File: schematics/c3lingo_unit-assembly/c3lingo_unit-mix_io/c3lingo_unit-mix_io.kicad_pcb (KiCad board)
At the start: 2 copper layers, 80 x 50 mm, 47 parts, among them J201 Stage Line-In, J202 Mix Line-Out, J203 PowerSupply, J204 Ch1, J205 Ch2, J206 Ch3, SW201 GND Lift, U201 LM833-N, U202 DRV135UA, U203 LM833-N

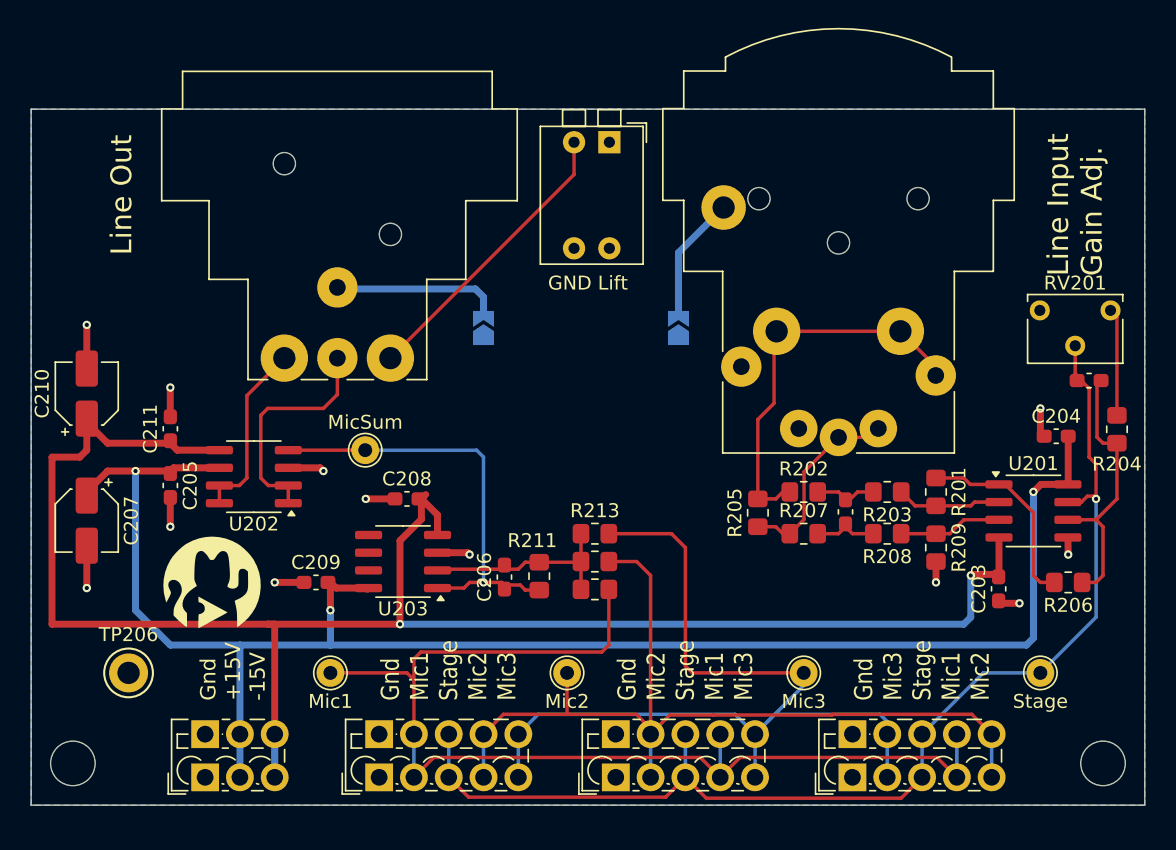
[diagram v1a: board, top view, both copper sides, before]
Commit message: Line I/O: Optimize Schematic and update PCB
Share one LM833 instead of only using one half for summing and line input each.
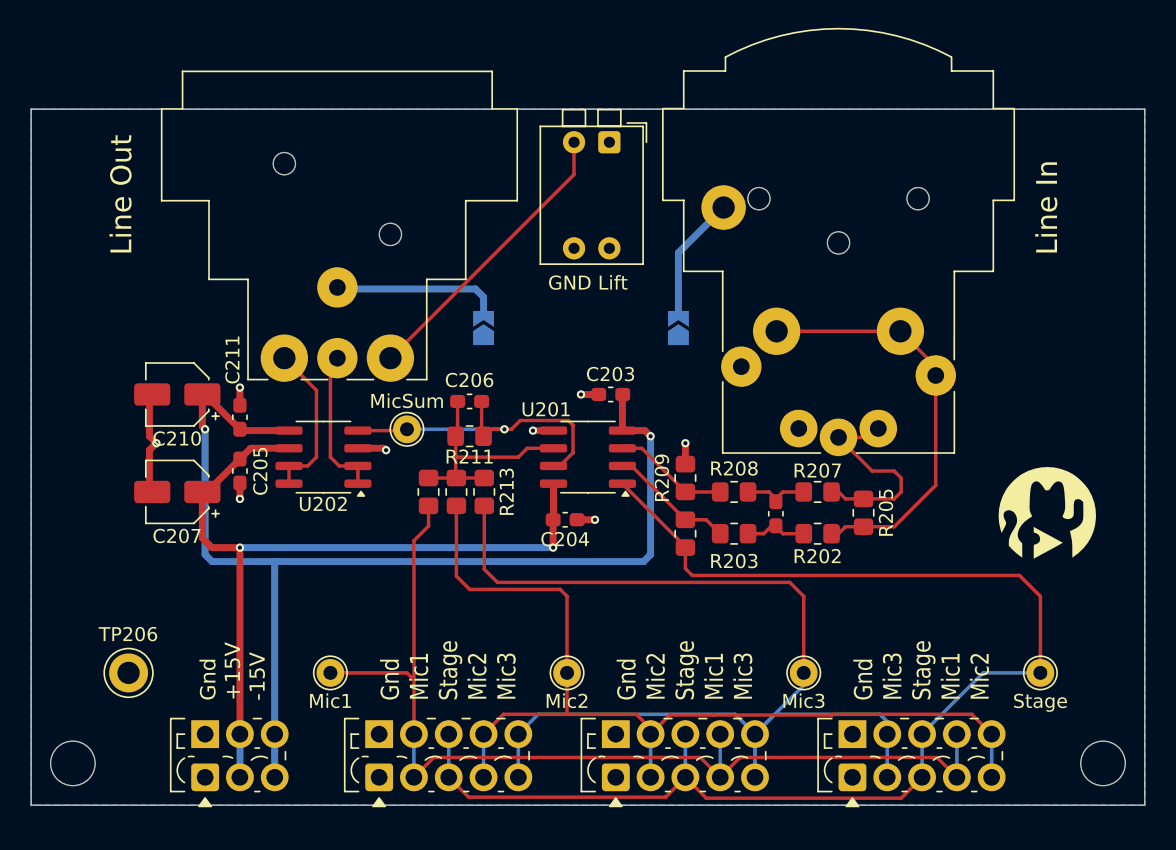
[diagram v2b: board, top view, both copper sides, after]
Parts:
- removed C201: 47pF, Capacitor_SMD:C_0603_1608Metric_Pad1.08x0.95mm_HandSolder
- removed C208, C209: 100nF, Capacitor_SMD:C_0603_1608Metric_Pad1.08x0.95mm_HandSolder
- removed R204: 22K, Resistor_SMD:R_0805_2012Metric_Pad1.20x1.40mm_HandSolder
- removed R206: 47K, Resistor_SMD:R_0805_2012Metric_Pad1.20x1.40mm_HandSolder
- removed RV201: 100K, Potentiometer_THT:Potentiometer_Vishay_T73XX_Horizontal
- removed U203: LM833-N, Package_SO:SOIC-8_3.9x4.9mm_P1.27mm
- R211: value 22K -> 10K
- moved G*** 60.2 mm to (133.0, 79.0)
- moved C204 35.8 mm to (98.4, 79.5), turned to 180 degrees
- moved U201 32.2 mm to (100.0, 75.0), turned to 180 degrees
- moved C203 31.2 mm to (101.6, 70.5), turned to 0 degrees
- moved R209 18.7 mm to (107.0, 76.5), turned to 90 degrees
- moved R201 18.2 mm to (107.0, 80.5), turned to 90 degrees
- moved R210 13.8 mm to (88.5, 77.5), turned to -90 degrees
- moved C206 12.9 mm to (91.5, 71.0), turned to 180 degrees
- moved R203 11.4 mm to (110.5, 80.5), turned to 0 degrees
- moved R208 11.4 mm to (110.5, 77.5), turned to 0 degrees
- moved R211 11.2 mm to (91.5, 73.5), turned to 180 degrees
- moved R212 11.1 mm to (90.5, 77.5), turned to -90 degrees
- moved R213 8.50 mm to (92.5, 77.5), turned to -90 degrees
- moved R205 7.59 mm to (119.8, 79.0), turned to -90 degrees
- moved C207 6.82 mm to (70.5, 77.5), turned to 180 degrees
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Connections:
- C206 pad 2: Net-(U203A--) -> Net-(U201B--)
- R201 pad 1: Net-(R201-Pad1) -> /Stage
- R210 pad 1: Net-(U203A--) -> Net-(U201B--)
- R211 pad 2: Net-(U203A--) -> Net-(U201B--)
- R212 pad 1: Net-(U203A--) -> Net-(U201B--)
- R213 pad 1: Net-(U203A--) -> Net-(U201B--)
- U201 pad 1: Net-(R201-Pad1) -> /Stage
- U201 pad 7: /Stage -> Net-(U202-VIN)
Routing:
- net +15V: track 119.2 -> 57.7 mm, vias 3 -> 2
- net -15V: track 125.6 -> 80.2 mm
- net Net-(U203A--): track 15.5 -> 0.00 mm
- net Net-(R201-Pad1): track 14.3 -> 0.00 mm
- net /Stage: track 84.1 -> 95.8 mm, vias 1 -> 0
- net /Mic_Ch3: track 67.7 -> 78.3 mm
- net Net-(R204-Pad1): track 7.73 -> 0.00 mm
- net Net-(U202-VIN): track 31.1 -> 23.9 mm
- net /Mic_Ch1: track 81.1 -> 74.2 mm
- net GND: track 24.6 -> 17.7 mm, vias 12 -> 8
- net Net-(U202-SENSE-): track 16.7 -> 10.8 mm
- net /Mic_Ch2: track 65.8 -> 70.1 mm
- net Net-(U201B--): track 20.7 -> 16.9 mm
- net Net-(J201-Pad2): track 28.2 -> 30.2 mm
- net Net-(U202-SENSE+): track 13.2 -> 11.6 mm
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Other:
- board text added: "Line In"
- board text added: "c3lingo Interpreter Unit Mix I/O v0.4.0-dev 2025-08-25"
- board text removed: "Line Input Gain Adj."
- board text removed: "c3lingo Interpreter Unit Mix I/O v0.3.3 2024-09-08"

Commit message: Change inter-PCB connections to IDC connectors
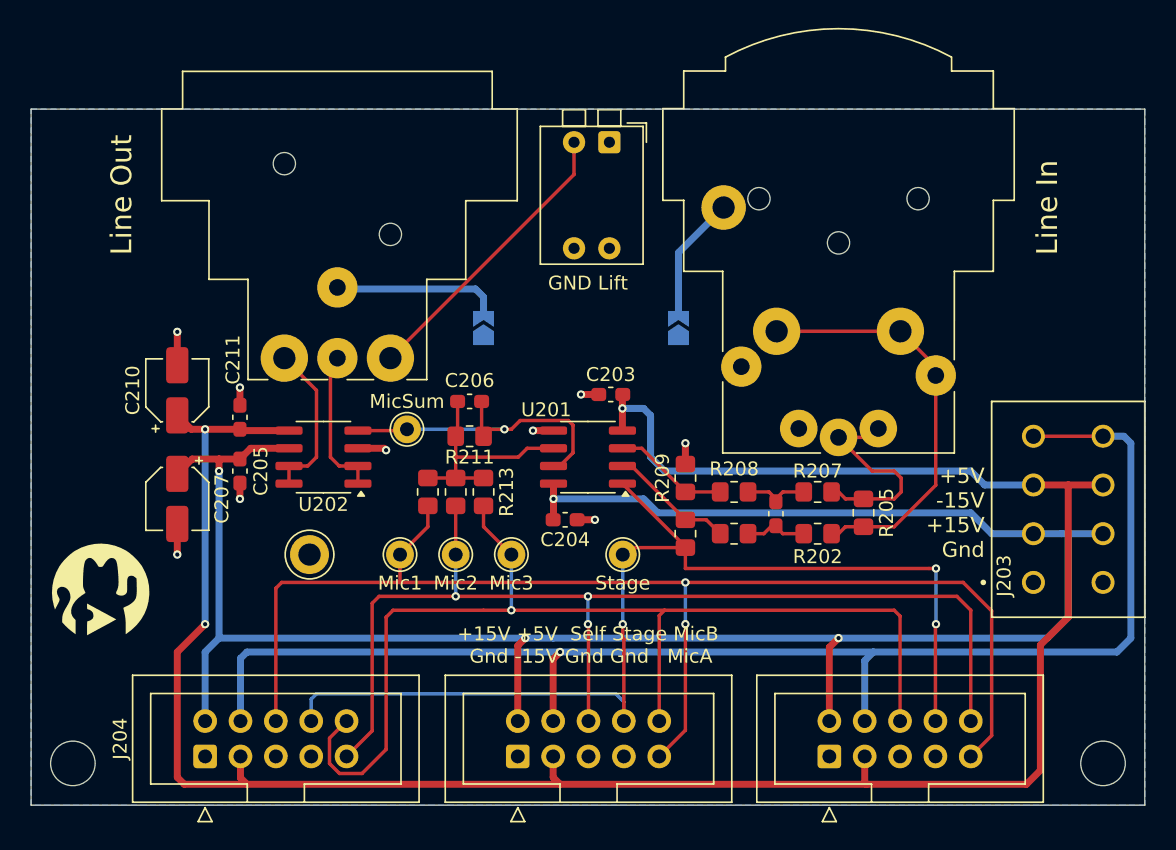
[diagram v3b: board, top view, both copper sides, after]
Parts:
- J203: footprint TerminalBlock_Phoenix:TerminalBlock_Phoenix_PTSM-0,5-3-2.5-V-THR_1x03_P2.50mm_Vertical -> c3lingo_unit-footprints:TerminalBlock_Phoenix_SPTAF-1-4-3.5_1x04_P3.5mm
- J204, J205, J206: footprint TerminalBlock_Phoenix:TerminalBlock_Phoenix_PTSM-0,5-5-2.5-V-THR_1x05_P2.50mm_Vertical -> Connector_IDC:IDC-Header_2x05_P2.54mm_Vertical
- moved J203 68.5 mm to (140.0, 86.5), turned to 90 degrees
- moved G*** 68.2 mm to (65.0, 84.5)
- moved TP201 31.2 mm to (102.5, 82.0)
- moved TP205 22.7 mm to (94.5, 82.0)
- moved TP206 15.5 mm to (80.0, 82.0)
- moved J204 12.6 mm to (72.5, 96.5), turned to 90 degrees
- moved TP203 11.7 mm to (90.5, 82.0)
- moved TP202 9.86 mm to (86.5, 82.0)
- moved J205 7.20 mm to (95.0, 96.5), turned to 90 degrees
- moved J206 2.24 mm to (117.3, 96.5), turned to 90 degrees
- moved C207 0.50 mm to (70.5, 78.0), turned to -90 degrees
- moved C210 0.30 mm to (70.5, 70.2), turned to 90 degrees
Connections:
- J204 pad 2: /Mic_Ch1 -> +15V
- J204 pad 3: /Stage -> -15V
- J204 pad 4: /Mic_Ch2 -> +5V
- J204 pad 5: /Mic_Ch3 -> GND
- J205 pad 2: /Mic_Ch2 -> +15V
- J205 pad 3: /Stage -> -15V
- J205 pad 4: /Mic_Ch1 -> +5V
- J205 pad 5: /Mic_Ch3 -> GND
- J206 pad 2: /Mic_Ch3 -> +15V
- J206 pad 3: /Stage -> -15V
- J206 pad 4: /Mic_Ch1 -> +5V
- J206 pad 5: /Mic_Ch2 -> GND
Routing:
- net +5V: track 0.00 -> 100.7 mm, vias 0 -> 1
- net +15V: track 57.7 -> 151.2 mm, vias 2 -> 4
- net -15V: track 80.2 -> 165.9 mm, vias 2 -> 3
- net /Mic_Ch1: track 74.2 -> 92.7 mm, vias 0 -> 2
- net /Stage: track 95.8 -> 79.3 mm, vias 0 -> 3
- net /Mic_Ch2: track 70.1 -> 78.8 mm, vias 0 -> 3
- net GND: track 17.7 -> 14.6 mm, vias 8 -> 9
- net /Mic_Ch3: track 78.3 -> 79.4 mm, vias 0 -> 1
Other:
- board text added: "+15V +5V Self Stage MicB Gnd -15V Gnd Gnd MicA"
- board text added: "+5V -15V +15V Gnd"
- board text added: "c3lingo Interpreter Unit Mix I/O v0.4.0 2025-08-26"
- board text removed: "Gnd +15V -15V"
- board text removed: "Gnd Mic1 Stage Mic2 Mic3"
- board text removed: "Gnd Mic2 Stage Mic1 Mic3"
- board text removed: "Gnd Mic3 Stage Mic1 Mic2"
- board text removed: "c3lingo Interpreter Unit Mix I/O v0.4.0-dev 2025-08-25"

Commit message: Line I/O: Fix polarity of C210
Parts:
- turned C210 to -90 degrees
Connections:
- C210 pad 1: -15V -> GND
- C210 pad 2: GND -> -15V
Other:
- board text added: "c3lingo Interpreter Unit Mix I/O v0.4.1 2025-09-08"
- board text removed: "c3lingo Interpreter Unit Mix I/O v0.4.0 2025-08-26"
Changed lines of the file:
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@@
 	(title_block
 		(title "c3lingo interpeter unit -- main I/O")
-		(date "2025-08-26")
-		(rev "v0.4.0")
+		(date "2025-09-08")
+		(rev "v0.4.1")
 		(company "Jannik Beyerstedt (jtbx)")
 		(comment 1 "Prototype 3")
@@
 	(footprint "Capacitor_SMD:CP_Elec_4x5.4"
 		(layer "F.Cu")
-		(at 70.5 70.2 90)
+		(at 70.5 70.2 -90)
 		(descr "SMD capacitor, aluminum electrolytic, Panasonic A5 / Nichicon, 4.0x5.4mm")
 		(tags "capacitor electrolytic")
@@
 		)
 		(property "Datasheet" "~"
-			(at 0 0 90)
+			(at 0 0 270)
 			(unlocked yes)
 			(layer "F.Fab")
@@
 		)
 		(property "Description" ""
-			(at 0 0 90)
+			(at 0 0 270)
 			(unlocked yes)
 			(layer "F.Fab")
@@
 		)
 		(property "Model" "25V+"
-			(at 0 0 90)
+			(at 0 0 270)
 			(unlocked yes)
 			(layer "F.Fab")
@@
 		)
 		(property "LCSC Part #" "C3343"
-			(at 0 0 90)
+			(at 0 0 270)
 			(unlocked yes)
 			(layer "F.Fab")
@@
 		)
 		(property "FT Rotation Offset" "180"
-			(at 0 0 0)
+			(at 0 0 180)
 			(unlocked yes)
 			(layer "F.Fab")
@@
 		(attr smd)
 		(fp_line
-			(start 2.26 -2.26)
-			(end 2.26 -1.06)
+			(start -1.195563 2.26)
+			(end 2.26 2.26)
 			(stroke
 				(width 0.12)
@@
 		)
 		(fp_line
-			(start -1.195563 -2.26)
-			(end 2.26 -2.26)
+			(start 2.26 2.26)
+			(end 2.26 1.06)
 			(stroke
 				(width 0.12)
@@
 		)
 		(fp_line
-			(start -2.75 -1.81)
-			(end -2.75 -1.31)
+			(start -2.26 1.195563)
+			(end -1.195563 2.26)
 			(stroke
 				(width 0.12)
@@
 		)
 		(fp_line
-			(start -3 -1.56)
-			(end -2.5 -1.56)
+			(start -2.26 1.195563)
+			(end -2.26 1.06)
 			(stroke
 				(width 0.12)
@@
 		(fp_line
 			(start -2.26 -1.195563)
-			(end -1.195563 -2.26)
+			(end -2.26 -1.06)
 			(stroke
 				(width 0.12)
@@
 		(fp_line
 			(start -2.26 -1.195563)
-			(end -2.26 -1.06)
+			(end -1.195563 -2.26)
 			(stroke
 				(width 0.12)
@@
 		)
 		(fp_line
-			(start -2.26 1.195563)
-			(end -2.26 1.06)
+			(start -3 -1.56)
+			(end -2.5 -1.56)
 			(stroke
 				(width 0.12)
@@
 		)
 		(fp_line
-			(start -2.26 1.195563)
-			(end -1.195563 2.26)
+			(start -2.75 -1.81)
+			(end -2.75 -1.31)
 			(stroke
 				(width 0.12)
@@
 		)
 		(fp_line
-			(start 2.26 2.26)
-			(end 2.26 1.06)
+			(start -1.195563 -2.26)
+			(end 2.26 -2.26)
 			(stroke
 				(width 0.12)
@@
 		)
 		(fp_line
-			(start -1.195563 2.26)
-			(end 2.26 2.26)
+			(start 2.26 -2.26)
+			(end 2.26 -1.06)
 			(stroke
 				(width 0.12)
@@
 		)
 		(fp_line
-			(start 2.4 -2.4)
-			(end 2.4 -1.05)
+			(start -1.25 2.4)
+			(end 2.4 2.4)
 			(stroke
 				(width 0.05)
@@
 		)
 		(fp_line
-			(start -1.25 -2.4)
-			(end 2.4 -2.4)
+			(start -2.4 1.25)
+			(end -1.25 2.4)
 			(stroke
 				(width 0.05)
@@
 		)
 		(fp_line
-			(start -2.4 -1.25)
-			(end -1.25 -2.4)
+			(start -3.35 1.05)
+			(end -2.4 1.05)
 			(stroke
 				(width 0.05)
@@
 		)
 		(fp_line
-			(start -2.4 -1.25)
-			(end -2.4 -1.05)
+			(start -2.4 1.05)
+			(end -2.4 1.25)
 			(stroke
 				(width 0.05)
@@
 		)
 		(fp_line
-			(start 3.35 -1.05)
-			(end 3.35 1.05)
+			(start 2.4 1.05)
+			(end 2.4 2.4)
 			(stroke
 				(width 0.05)
@@
 		)
 		(fp_line
-			(start 2.4 -1.05)
-			(end 3.35 -1.05)
+			(start 3.35 1.05)
+			(end 2.4 1.05)
 			(stroke
 				(width 0.05)
@@
 		)
 		(fp_line
-			(start -2.4 -1.05)
-			(end -3.35 -1.05)
+			(start -3.35 -1.05)
+			(end -3.35 1.05)
 			(stroke
 				(width 0.05)
@@
 		)
 		(fp_line
-			(start -3.35 -1.05)
-			(end -3.35 1.05)
+			(start -2.4 -1.05)
+			(end -3.35 -1.05)
 			(stroke
 				(width 0.05)
@@
 		)
 		(fp_line
-			(start 3.35 1.05)
-			(end 2.4 1.05)
+			(start 2.4 -1.05)
+			(end 3.35 -1.05)
 			(stroke
 				(width 0.05)
@@
 		)
 		(fp_line
-			(start 2.4 1.05)
-			(end 2.4 2.4)
+			(start 3.35 -1.05)
+			(end 3.35 1.05)
 			(stroke
 				(width 0.05)
@@
 		)
 		(fp_line
-			(start -2.4 1.05)
-			(end -2.4 1.25)
+			(start -2.4 -1.25)
+			(end -2.4 -1.05)
 			(stroke
 				(width 0.05)
@@
 		)
 		(fp_line
-			(start -3.35 1.05)
-			(end -2.4 1.05)
+			(start -2.4 -1.25)
+			(end -1.25 -2.4)
 			(stroke
 				(width 0.05)
@@
 		)
 		(fp_line
-			(start -2.4 1.25)
-			(end -1.25 2.4)
+			(start -1.25 -2.4)
+			(end 2.4 -2.4)
 			(stroke
 				(width 0.05)
@@
 		)
 		(fp_line
-			(start -1.25 2.4)
-			(end 2.4 2.4)
+			(start 2.4 -2.4)
+			(end 2.4 -1.05)
 			(stroke
 				(width 0.05)
@@
 		)
 		(fp_line
-			(start 2.15 -2.15)
+			(start -1.15 2.15)
 			(end 2.15 2.15)
 			(stroke
@@
 		)
 		(fp_line
-			(start -1.15 -2.15)
-			(end 2.15 -2.15)
+			(start -2.15 1.15)
+			(end -1.15 2.15)
 			(stroke
 				(width 0.1)
@@
 		)
 		(fp_line
-			(start -1.374773 -1.2)
-			(end -1.374773 -0.8)
+			(start -1.574773 -1)
+			(end -1.174773 -1)
 			(stroke
 				(width 0.1)
@@
 		(fp_line
 			(start -2.15 -1.15)
-			(end -1.15 -2.15)
+			(end -2.15 1.15)
 			(stroke
 				(width 0.1)
@@
 		(fp_line
 			(start -2.15 -1.15)
-			(end -2.15 1.15)
+			(end -1.15 -2.15)
 			(stroke
 				(width 0.1)
@@
 		)
 		(fp_line
-			(start -1.574773 -1)
-			(end -1.174773 -1)
+			(start -1.374773 -1.2)
+			(end -1.374773 -0.8)
 			(stroke
 				(width 0.1)
@@
 		)
 		(fp_line
-			(start -2.15 1.15)
-			(end -1.15 2.15)
+			(start -1.15 -2.15)
+			(end 2.15 -2.15)
 			(stroke
 				(width 0.1)
@@
 		)
 		(fp_line
-			(start -1.15 2.15)
+			(start 2.15 -2.15)
 			(end 2.15 2.15)
 			(stroke
@@
 		)
 		(pad "1" smd roundrect
-			(at -1.8 0 90)
+			(at -1.8 0 270)
 			(size 2.6 1.6)
 			(layers "F.Cu" "F.Mask" "F.Paste")
 			(roundrect_rratio 0.15625)
-			(net 1 "-15V")
+			(net 3 "GND")
 			(pintype "passive")
 		)
 		(pad "2" smd roundrect
-			(at 1.8 0 90)
+			(at 1.8 0 270)
 			(size 2.6 1.6)
 			(layers "F.Cu" "F.Mask" "F.Paste")
 			(roundrect_rratio 0.15625)
-			(net 3 "GND")
+			(net 1 "-15V")
 			(pintype "passive")
 		)
@@
 		)
 	)
-	(gr_text "c3lingo Interpreter Unit\nMix I/O\nv0.4.0 2025-08-26"
+	(gr_text "c3lingo Interpreter Unit\nMix I/O\nv0.4.1 2025-09-08"
 		(at 100.5 88 0)
 		(layer "B.SilkS")

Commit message: WIP: Add some artwork to the PCBs
TODO: OSHW
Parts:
- added G***: LOGO, c3lingo_unit-footprints:chaosknoten-10mm, F.Cu at (100.5, 68.2)
- added G***: LOGO, c3lingo_unit-footprints:catears-10mm, B.Cu at (85.0, 80.0)
- added G***: LOGO, c3lingo_unit-footprints:antifa-10mm, B.Cu at (117.0, 80.0)
